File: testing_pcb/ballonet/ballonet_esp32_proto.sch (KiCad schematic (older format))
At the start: 14 parts, among them M1 Motor_DC, M2 Motor_DC, U1 DOIT-ESP32-DEVKIT-V1-30, U2 GY-291-ADXL345-breakoout, U3 CJVL53L0XV2-VL53L0X-breakout, U4 Adafruit-BMP388-breakout, U5 Adafruit-DRV8833-breakout, U6 Polulu-S7V8F3-3V3

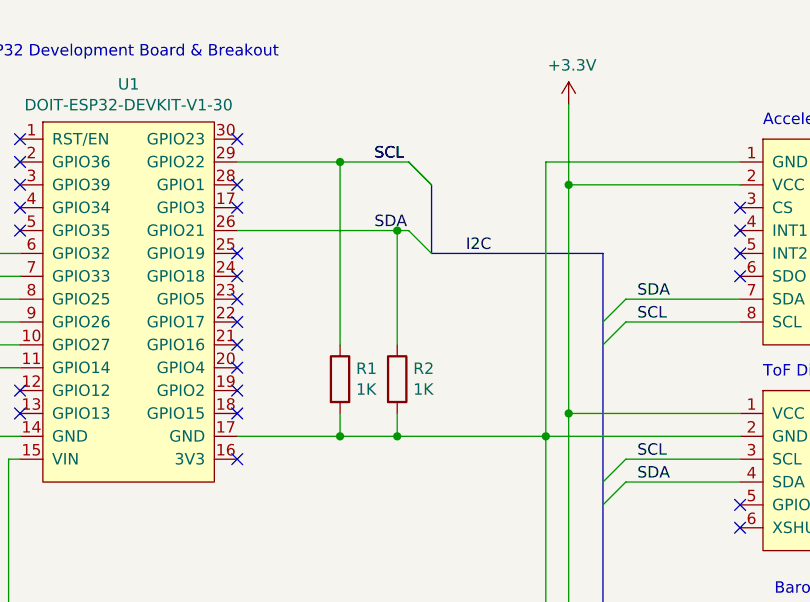
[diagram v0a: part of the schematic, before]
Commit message: added 40mm vane pump files
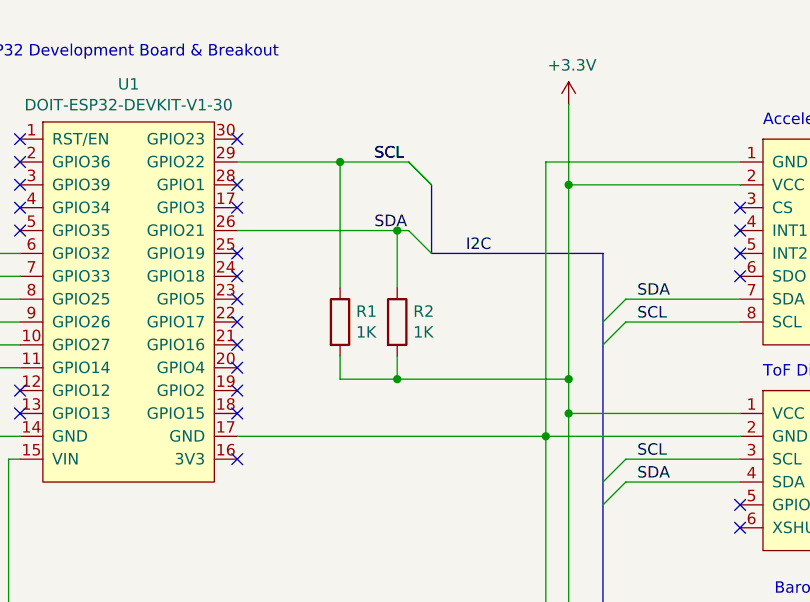
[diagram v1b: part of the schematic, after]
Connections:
- wire segments 91 -> 92
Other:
- moved on the sheet: R1, R2
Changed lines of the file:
@@
 L Device:R R1
 U 1 1 605A92F4
-P 3350 2450
-F 0 "R1" H 3420 2496 50  0000 L CNN
-F 1 "1K" H 3420 2405 50  0000 L CNN
-F 2 "" V 3280 2450 50  0001 C CNN
-F 3 "~" H 3350 2450 50  0001 C CNN
-	1    3350 2450
+P 3350 2200
+F 0 "R1" H 3420 2246 50  0000 L CNN
+F 1 "1K" H 3420 2155 50  0000 L CNN
+F 2 "" V 3280 2200 50  0001 C CNN
+F 3 "~" H 3350 2200 50  0001 C CNN
+	1    3350 2200
 	1    0    0    -1
 $EndComp
@@
 L Device:R R2
 U 1 1 605AA82F
-P 3600 2450
-F 0 "R2" H 3670 2496 50  0000 L CNN
-F 1 "1K" H 3670 2405 50  0000 L CNN
-F 2 "" V 3530 2450 50  0001 C CNN
-F 3 "~" H 3600 2450 50  0001 C CNN
-	1    3600 2450
+P 3600 2200
+F 0 "R2" H 3670 2246 50  0000 L CNN
+F 1 "1K" H 3670 2155 50  0000 L CNN
+F 2 "" V 3530 2200 50  0001 C CNN
+F 3 "~" H 3600 2200 50  0001 C CNN
+	1    3600 2200
 	1    0    0    -1
 $EndComp
@@
 	3600 1800 3650 1800
 Wire Wire Line
-	3350 2300 3350 1500
+	3350 2050 3350 1500
 Connection ~ 3350 1500
 Wire Wire Line
@@
 Connection ~ 4350 2600
 Wire Wire Line
-	4350 2600 4350 1600
+	4350 2600 4350 2450
 Entry Wire Line
 	4600 2800 4500 2900
@@
 	4250 3750 4250 3850
 Wire Wire Line
-	2900 2700 3350 2700
-Wire Wire Line
-	3600 1800 3600 2300
-Wire Wire Line
-	3350 2600 3350 2700
-Connection ~ 3350 2700
-Wire Wire Line
-	3350 2700 3600 2700
-Wire Wire Line
-	3600 2600 3600 2700
-Connection ~ 3600 2700
-Wire Wire Line
-	3600 2700 4250 2700
+	3600 1800 3600 2050
 Text Label 3900 1900 0    50   ~ 0
 I2C
@@
 Wire Wire Line
 	7700 2850 7700 3000
+Wire Wire Line
+	2900 2700 4250 2700
+Wire Wire Line
+	3350 2450 3350 2350
+Wire Wire Line
+	3350 2450 3600 2450
+Wire Wire Line
+	3600 2450 3600 2350
+Wire Wire Line
+	3600 2450 4350 2450
 Wire Bus Line
 	4500 1900 4500 4150
+Connection ~ 3600 2450
+Connection ~ 4350 2450
+Wire Wire Line
+	4350 2450 4350 1600
 $EndSCHEMATC

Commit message: updated schematic
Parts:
- removed C3: 10U, symbol Device:C
- removed U6: Polulu-S7V8F3-3V3, symbol adafruit-breakouts:Polulu-S7V8F3-3V3
- added M3: Valve_DC, symbol Motor:Motor_DC
- added U5: MB1240-000, symbol adafruit-breakouts:MB1240-000
- added U7: Adafruit-DRV8833-breakout, symbol adafruit-breakouts:Adafruit-DRV8833-breakout
- added U8: Adafruit-PowerBoost-1000C, symbol adafruit-breakouts:Adafruit-PowerBoost-1000C
- BT1: value 7.2V -> 3.8V
- renumbered U5 to U6
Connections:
- net labels added: +BATT, GPIO12, GPIO13, GPIO14, GPIO15, GPIO16, GPIO17, GPIO2, GPIO25, GPIO26, GPIO27, GPIO32, GPIO33, GPIO4, GPIO5
- net labels removed: 3V3
- wire segments 92 -> 103
- no-connect marks 33 -> 39
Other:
- note added: "Barometer / Thermometer\n"
- note added: "Laser ToF Rangefinder"
- note added: "Motor Driver 1\n"
- note added: "Motor Driver 2"
- note added: "Ultrasonic Rangefinder\n"
- note removed: "3.3V Buck-Boost Regulator"
- note removed: "7.2 V to 5 V motor stepdown"
- note removed: "Barometer / Height Gauge"
- note removed: "Motor Driver"
- note removed: "ToF Distance Sensor"
- moved on the sheet: BT1, C1, C2, M1, M2, U6
